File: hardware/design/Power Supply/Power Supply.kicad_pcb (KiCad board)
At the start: 2 copper layers, 127 x 62.2 mm, 33 parts, among them P1 CONN_2, P2 CONN_5, T1 161H34, U1 LM2596SX-3.3, U2 LM2596S-ADJ, U3 UA7815, U4 UA7915

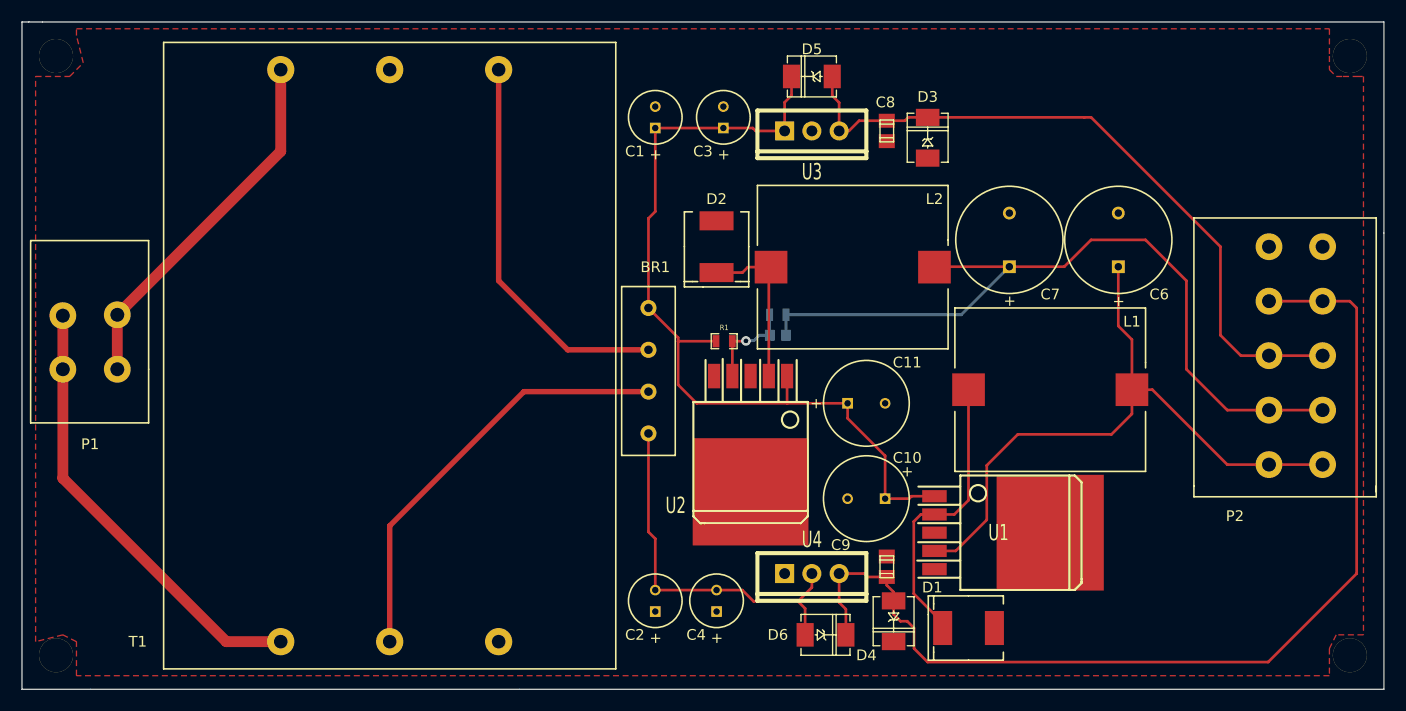
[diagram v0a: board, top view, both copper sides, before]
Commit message: Power Supply Design
Finished board routing and Gerber generation.
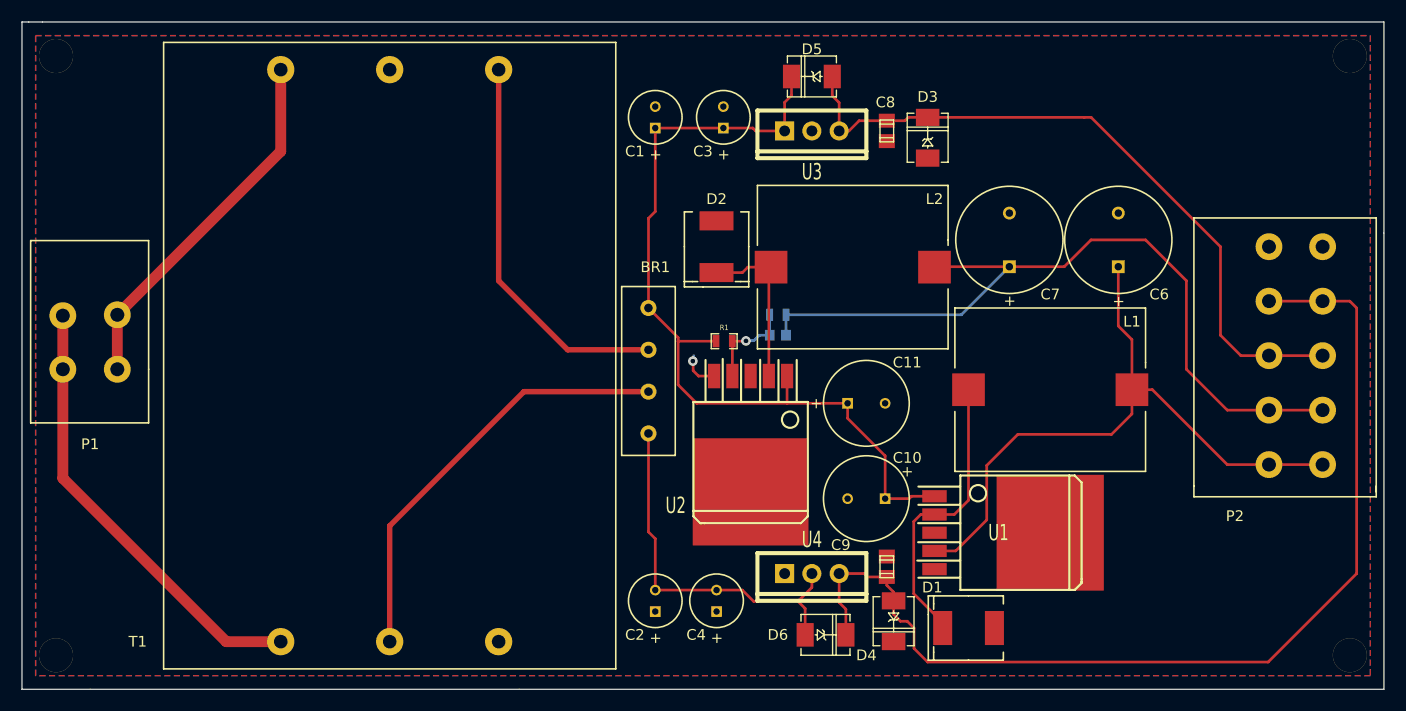
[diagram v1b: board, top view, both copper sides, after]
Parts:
- added VIA_OSHPARK: VAL**, VIA_OSHPARK, F.Cu at (221.5, 152.0)
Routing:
- net GND: track 0.00 -> 3.61 mm, vias 0 -> 1
- added copper zone on B.Cu, net GND
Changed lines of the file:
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@@
   (general
     (links 70)
-    (no_connects 1)
-    (area 156.524 113.990001 300.405714 188.408)
+    (no_connects 0)
+    (area 156.524 113.990001 300.405714 186.376)
     (thickness 1.6)
     (drawings 11)
-    (tracks 140)
+    (tracks 147)
     (zones 0)
-    (modules 33)
+    (modules 34)
     (nets 15)
   )
@@
     (mod_text_size 1 1)
     (mod_text_width 0.15)
-    (pad_size 3.175 3.175)
-    (pad_drill 3.175)
+    (pad_size 0.508 0.508)
+    (pad_drill 0.3302)
     (pad_to_mask_clearance 0)
     (aux_axis_origin 0 0)
-    (visible_elements FFFFFFBF)
+    (visible_elements 7FFFFFBF)
     (pcbplotparams
-      (layerselection 3178497)
+      (layerselection 284196865)
       (usegerberextensions true)
       (excludeedgelayer true)
@@
       (outputformat 1)
       (mirror false)
-      (drillshape 1)
+      (drillshape 0)
       (scaleselection 1)
-      (outputdirectory ""))
+      (outputdirectory "C:/Users/William/Documents/GitHub/P14345/hardware/design/Power Supply/Gerbers/"))
   )
   (net 0 "")
@@
       (effects (font (size 1 1) (thickness 0.15)))
     )
-    (fp_text value 161H34 (at 0 35.052) (layer F.SilkS) hide
+    (fp_text value 161H34 (at 17.78 27.94) (layer F.SilkS) hide
       (effects (font (size 1 1) (thickness 0.15)))
     )
@@
       (layers *.Mask F.Cu F.SilkS)
       (clearance 1.27)
+    )
+  )
+  (module VIA_OSHPARK (layer F.Cu)
+    (at 221.4626 152.019)
+    (fp_text reference VIA_OSHPARK (at 0 3.81) (layer F.SilkS) hide
+      (effects (font (size 1 1) (thickness 0.15)))
+    )
+    (fp_text value VAL** (at 0 2.54) (layer F.SilkS) hide
+      (effects (font (size 1 1) (thickness 0.15)))
     )
   )
@@
   (gr_line (start 285.75 120.65) (end 285.75 140.335) (angle 90) (layer Edge.Cuts) (width 0.1))
   (gr_line (start 160.655 120.65) (end 285.75 120.65) (angle 90) (layer Edge.Cuts) (width 0.1))
+  (segment (start 223.29394 153.67) (end 221.8436 153.67) (width 0.254) (layer F.Cu) (net 1))
+  (segment (start 221.3864 152.1968) (end 221.3864 151.765) (width 0.254) (layer B.Cu) (net 1))
+  (segment (start 221.3102 152.273) (end 221.3864 152.1968) (width 0.254) (layer B.Cu) (net 1))
+  (via (at 221.3102 152.273) (size 0.889) (layers F.Cu B.Cu) (net 1))
+  (segment (start 221.3356 152.2984) (end 221.3102 152.273) (width 0.254) (layer F.Cu) (net 1))
+  (segment (start 221.3356 153.162) (end 221.3356 152.2984) (width 0.254) (layer F.Cu) (net 1))
+  (segment (start 221.8436 153.67) (end 221.3356 153.162) (width 0.254) (layer F.Cu) (net 1))
   (segment (start 239.24 165.1) (end 241.4778 165.1) (width 0.254) (layer F.Cu) (net 2))
   (segment (start 241.70386 164.87394) (end 243.84 164.87394) (width 0.254) (layer F.Cu) (net 2))
@@
     (polygon
       (pts
-        (xy 160.02 178.435) (xy 160.02 151.765) (xy 160.02 125.73) (xy 163.195 125.73) (xy 164.465 124.46)
-        (xy 163.83 121.92) (xy 163.83 121.285) (xy 280.67 121.285) (xy 280.67 123.825) (xy 280.67 125.095)
-        (xy 281.305 125.73) (xy 281.94 125.73) (xy 283.21 125.73) (xy 283.845 125.73) (xy 283.845 147.32)
-        (xy 283.845 177.8) (xy 281.305 177.8) (xy 280.67 179.07) (xy 280.67 181.61) (xy 163.83 181.61)
-        (xy 163.83 178.435) (xy 162.56 177.8) (xy 160.02 178.435)
+        (xy 284.48 181.61) (xy 160.02 181.61) (xy 160.02 121.92) (xy 284.48 121.92)
       )
     )
+  )
+  (zone (net 1) (net_name GND) (layer B.Cu) (hatch edge 0.508)
+    (connect_pads (clearance 0.508))
+    (min_thickness 0.254)
+    (fill (arc_segments 16) (thermal_gap 0.508) (thermal_bridge_width 0.508))
+    (polygon
+      (pts
+        (xy 284.48 181.61) (xy 160.02 181.61) (xy 160.02 121.92) (xy 284.48 121.92)
+      )
+    )

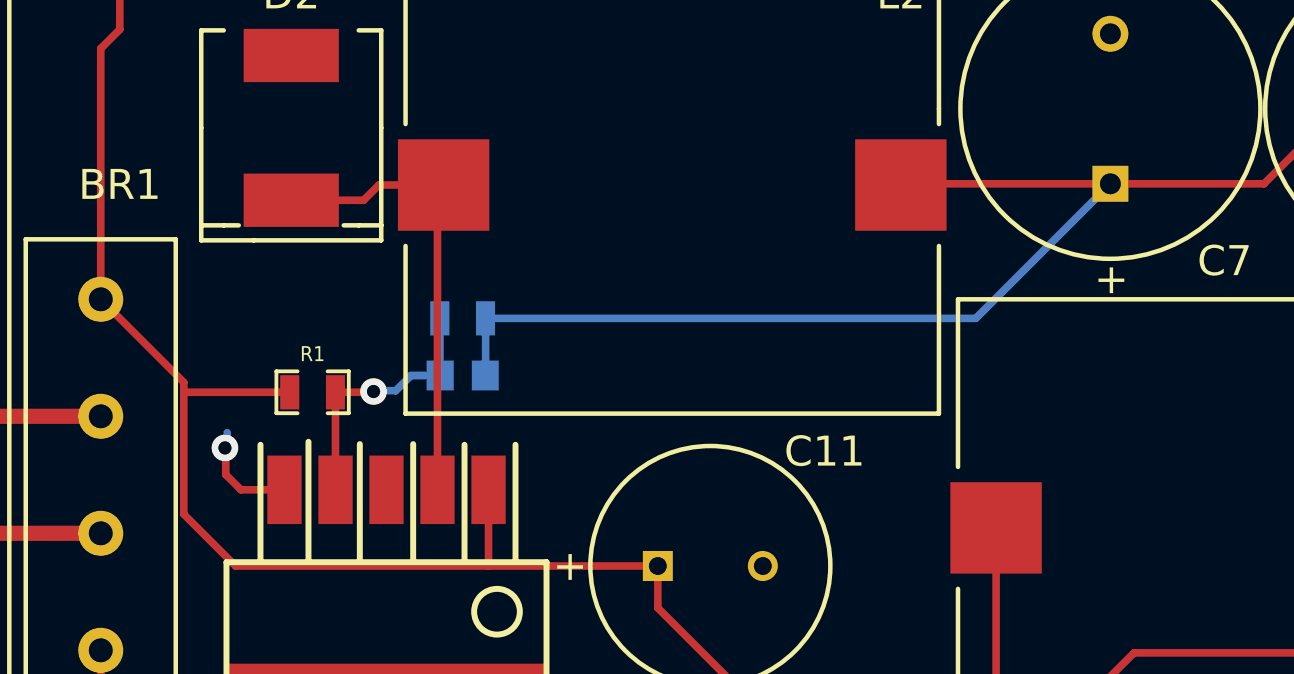
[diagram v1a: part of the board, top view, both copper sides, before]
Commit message: Power Supply Design
Working update. Changing 9V rail to 5V.
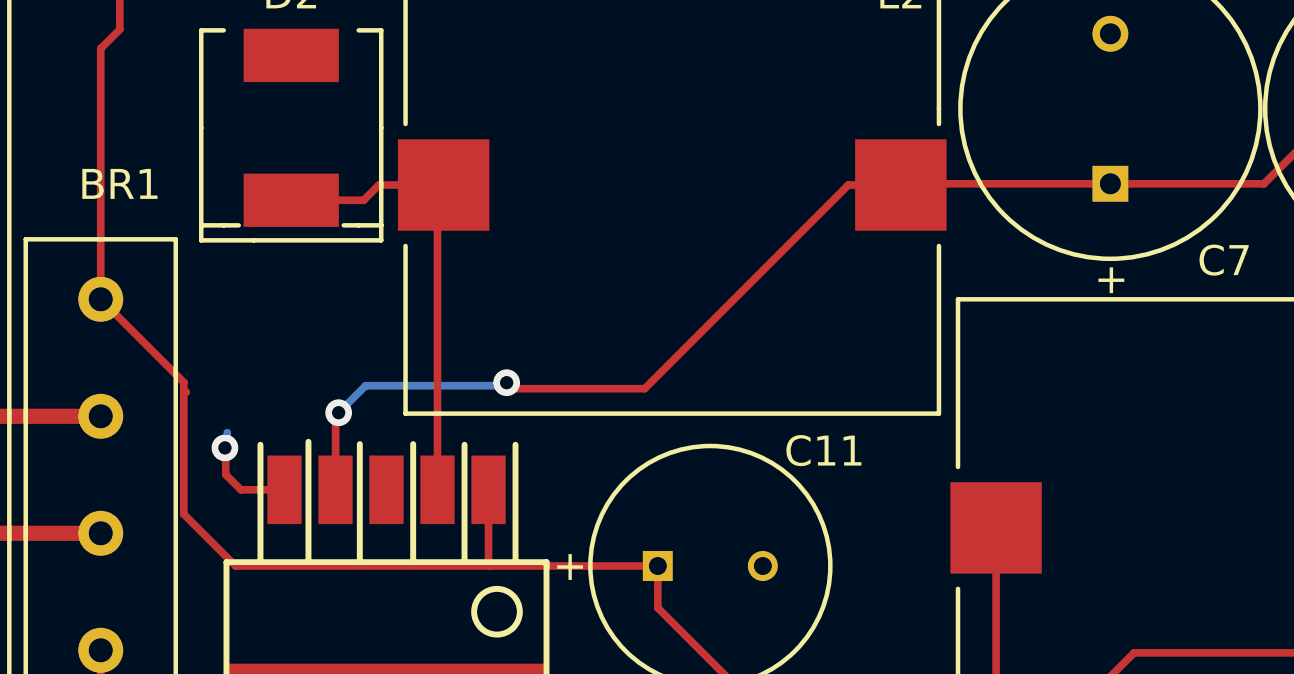
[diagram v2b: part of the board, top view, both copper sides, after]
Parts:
- removed C5: 1.5n, c_0603
- removed R1: 1K, SM0603_Resistor
- removed R2: 6.34K 1%, SM0603_Resistor
- U2: value LM2596S-ADJ -> LM2596S-5
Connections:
- C7 pad 1: N-0000012 -> N-000006
- L2 pad 2: N-0000012 -> N-000006
- P2 pad 2: N-0000012 -> N-000006
- U2 pad 4: N-0000010 (its old number) -> N-000006
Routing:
- net N-000006: track 0.00 -> 73.5 mm, vias 0 -> 2
- net N-0000012: track 73.3 -> 0.00 mm
- net N-0000010 (its old number): track 8.88 -> 0.00 mm, vias 1 -> 0
- net N-0000011: track 80.7 -> 77.1 mm

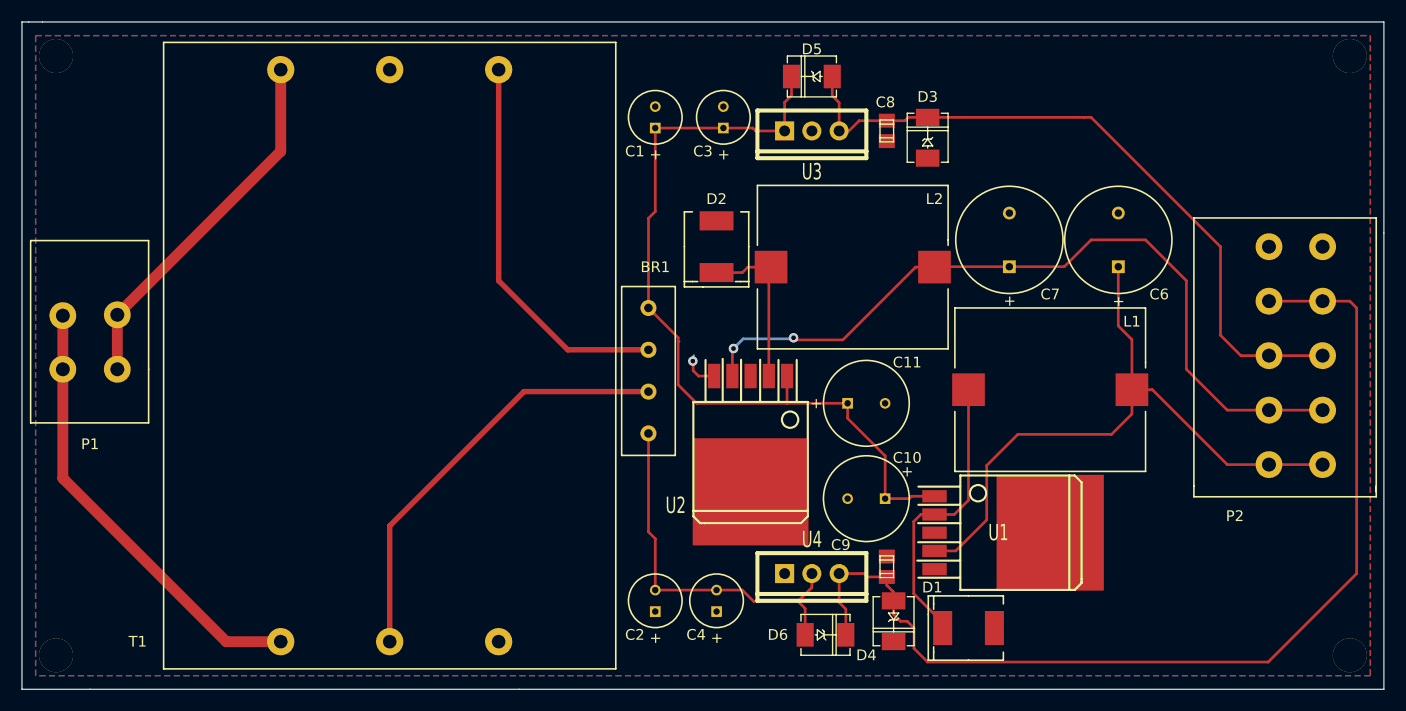
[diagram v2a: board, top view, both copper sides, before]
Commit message: Power Supply Design
Version 0.1 - Pilot release for review
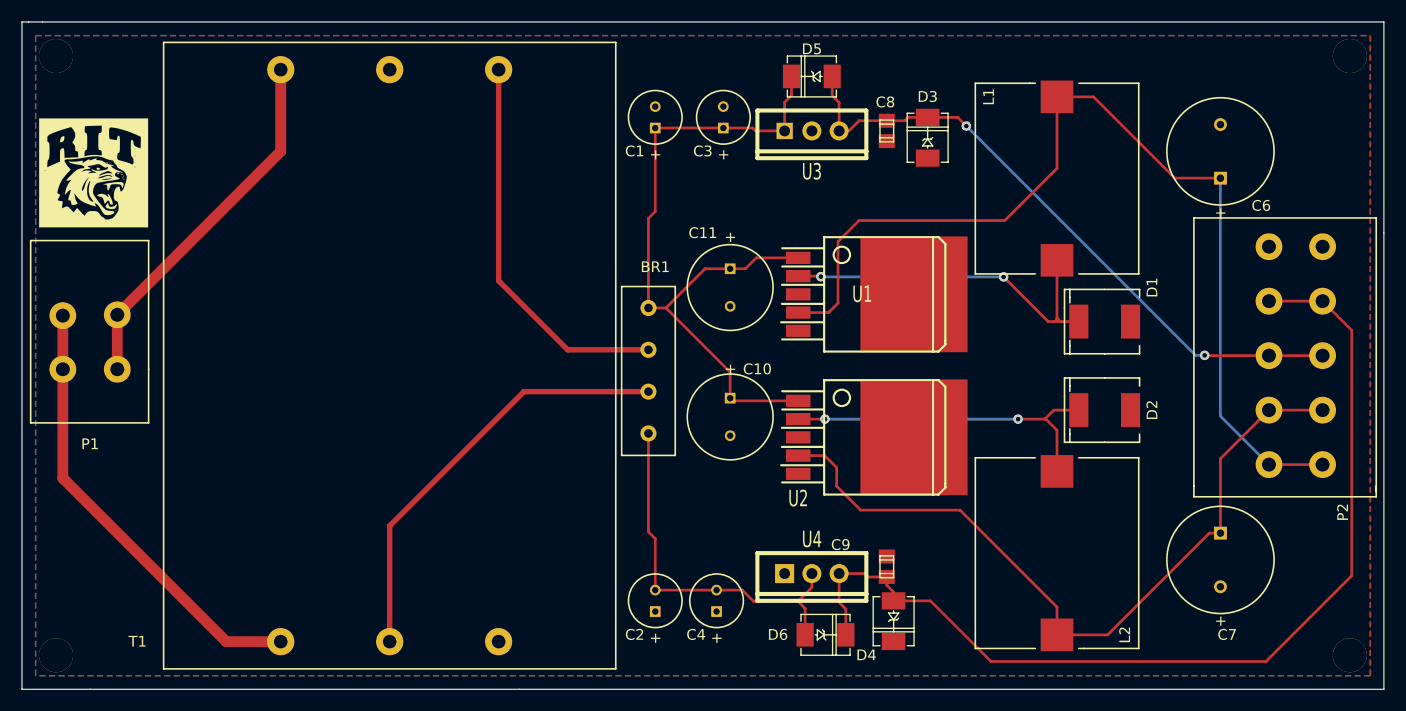
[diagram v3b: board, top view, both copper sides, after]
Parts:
- added G***: LOGO, LOGO, F.Cu at (165.4, 134.7)
- moved D2 39.3 mm to (259.7, 156.8), turned to 180 degrees
- moved C7 35.8 mm to (270.5, 170.8), turned to 270 degrees
- moved L2 32.8 mm to (255.3, 170.2), turned to 0 degrees
- moved D1 31.3 mm to (259.7, 148.6)
- moved U1 25.6 mm to (231.1, 146.1)
- moved L1 19.7 mm to (255.3, 135.3), turned to 180 degrees
- moved C11 16.7 mm to (224.8, 145.4), turned to 270 degrees
- moved C10 14.8 mm to (224.8, 157.5), turned to 270 degrees
- moved C6 12.6 mm to (270.5, 132.7)
- moved U2 7.24 mm to (231.1, 159.4), turned to 270 degrees
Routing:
- net N-000003: track 61.6 -> 91.7 mm
- net N-000009: track 15.5 -> 31.9 mm, vias 0 -> 2
- net N-0000011: track 77.1 -> 67.8 mm
- net N-0000014: track 27.3 -> 34.2 mm, vias 0 -> 2
- net N-000004: track 65.0 -> 60.2 mm, vias 0 -> 2
- net N-000005: track 97.1 -> 93.2 mm
- net GND: track 3.61 -> 0.00 mm, vias 1 -> 0
- net N-000006: track 73.5 -> 71.1 mm, vias 2 -> 0
